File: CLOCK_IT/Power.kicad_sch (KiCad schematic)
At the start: 31 parts, among them SW1 CK_KMS2xxG, U4 AXP2101, U5 MC-264

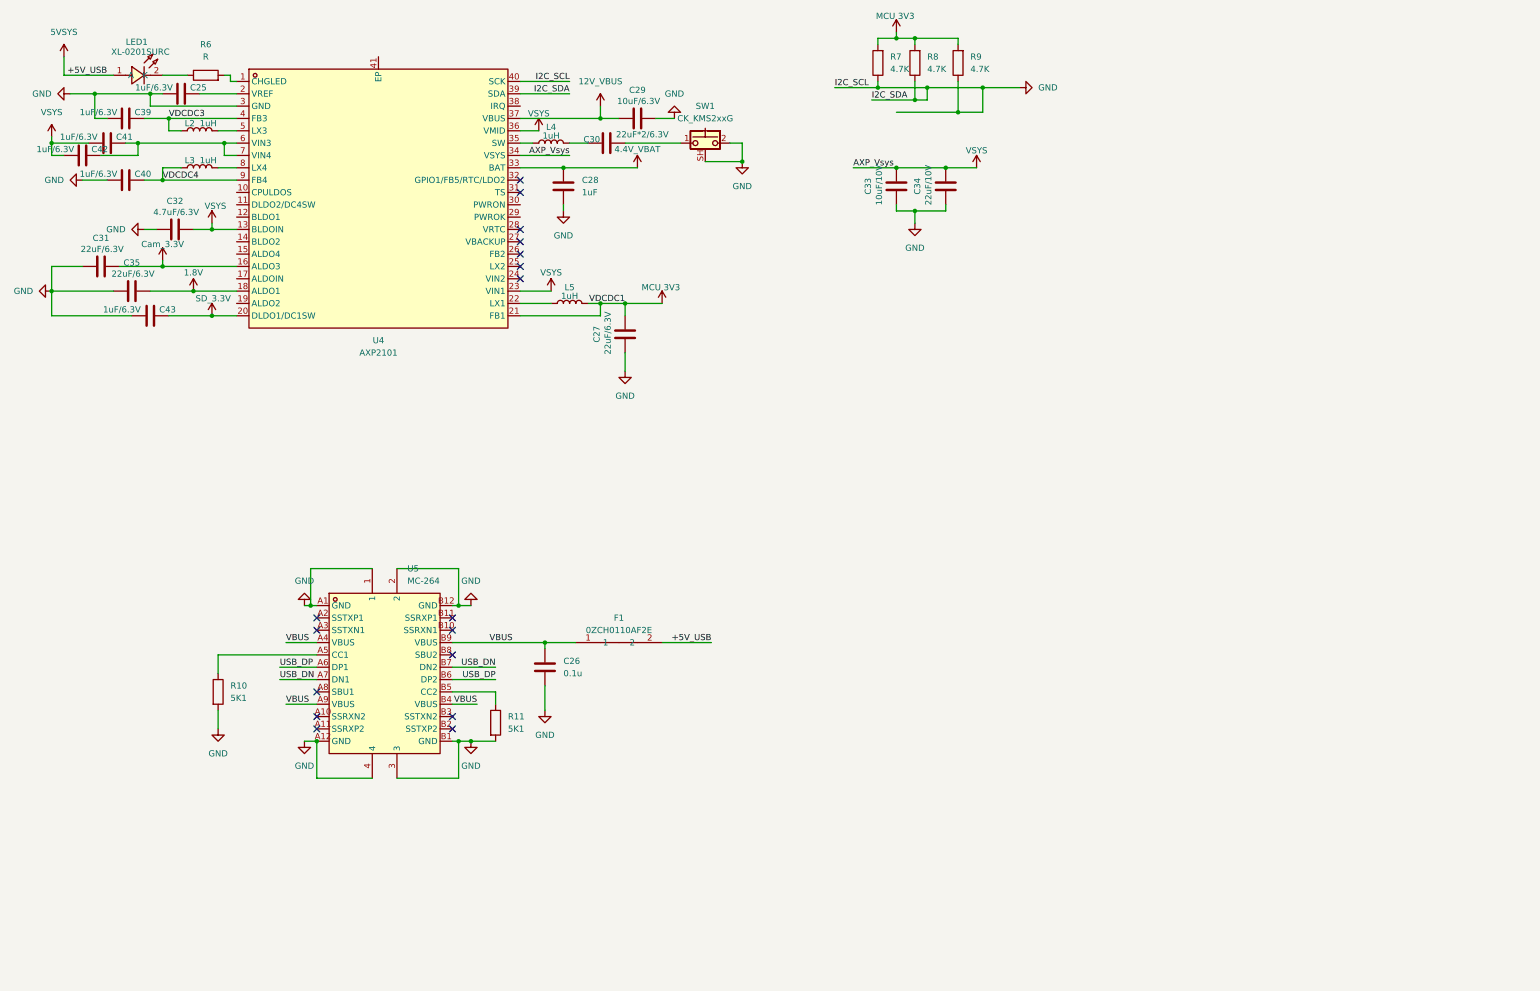
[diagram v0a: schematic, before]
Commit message: :fire: correcting PowerAXP and USB connection
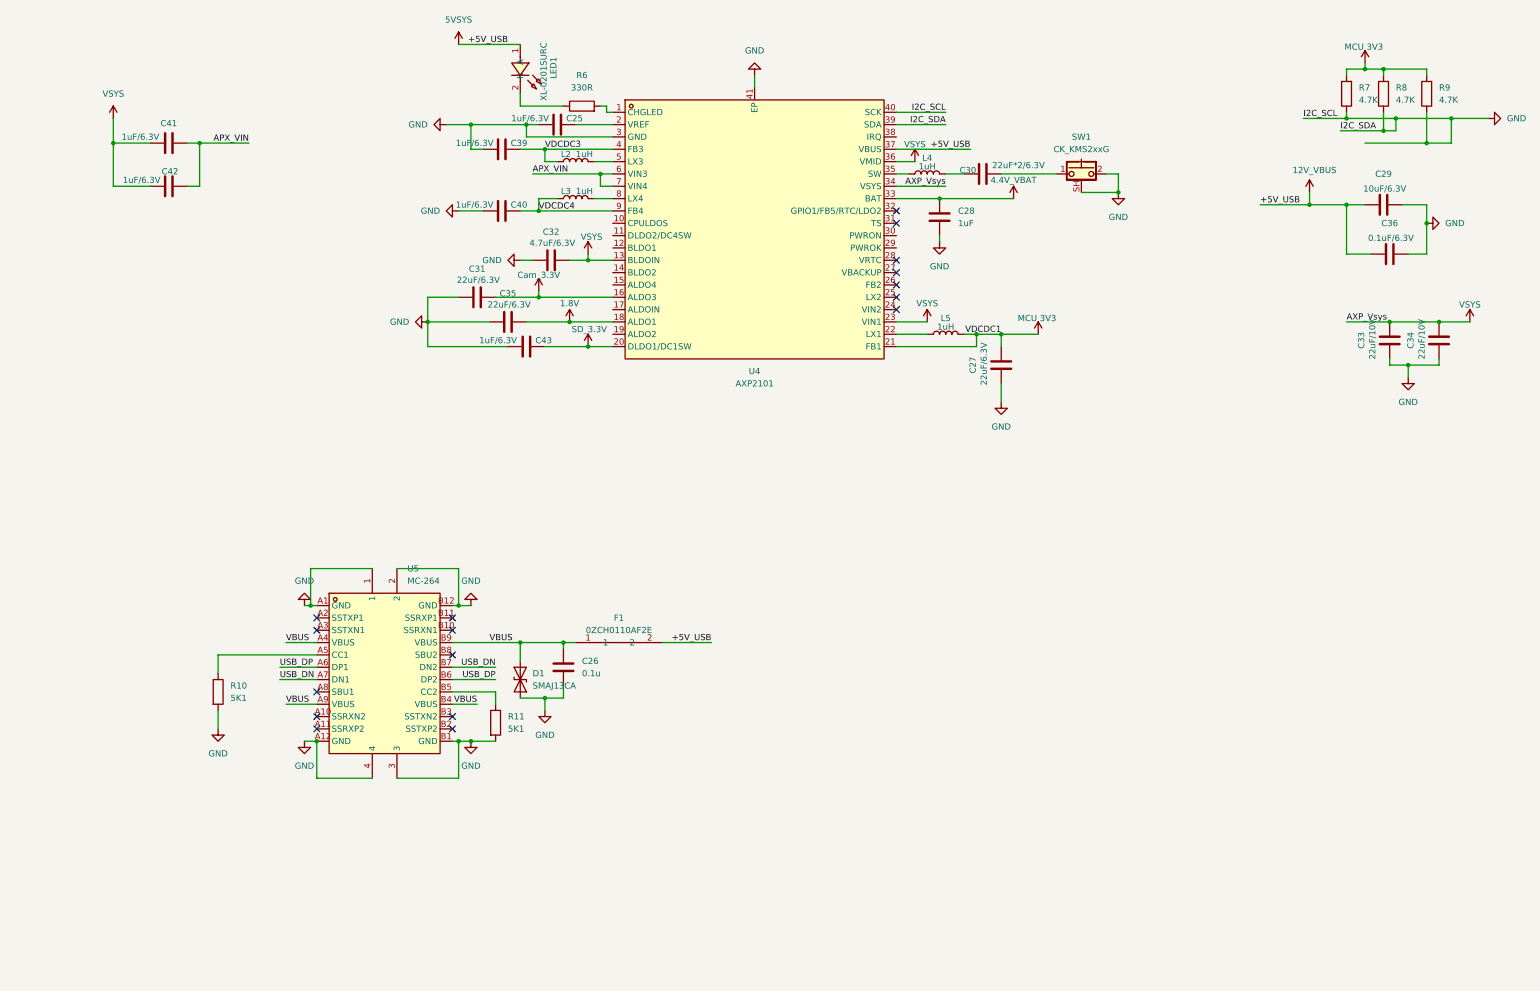
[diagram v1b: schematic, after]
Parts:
- added C36: 0.1uF/6.3V, symbol Device:C
- added D1: SMAJ13CA, Diode_SMD:D_SMA, symbol Diode:SMAJ13CA
- C33: value 10uF/10V -> 22uF/10V
- R6: value R -> 330R
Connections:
- net 5VSYS is gone; now on net 12V_VBUS: F1.2, LED1.1 (A)
- net 12V_VBUS: now also C36.1
- net GND: now also U4.41 (EP), C36.2, D1.1 (A1)
- net VBUS: now also D1.2 (A2)
- net APX_VIN: now reaches C41.2, C42.2, U4.6 (VIN3), U4.7 (VIN4)
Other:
- moved on the sheet: C25, C26, C27, C28, C29, C30, C31, C32, C33, C34, C35, C39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

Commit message: :art: small changes
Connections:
- net GND: now also U4.38 (IRQ)
- no-connect marks 17 -> 25
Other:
- moved on the sheet: C26, D1, F1, R10, R11, U5
